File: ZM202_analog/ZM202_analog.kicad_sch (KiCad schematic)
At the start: 2 parts, among them U2 LM324

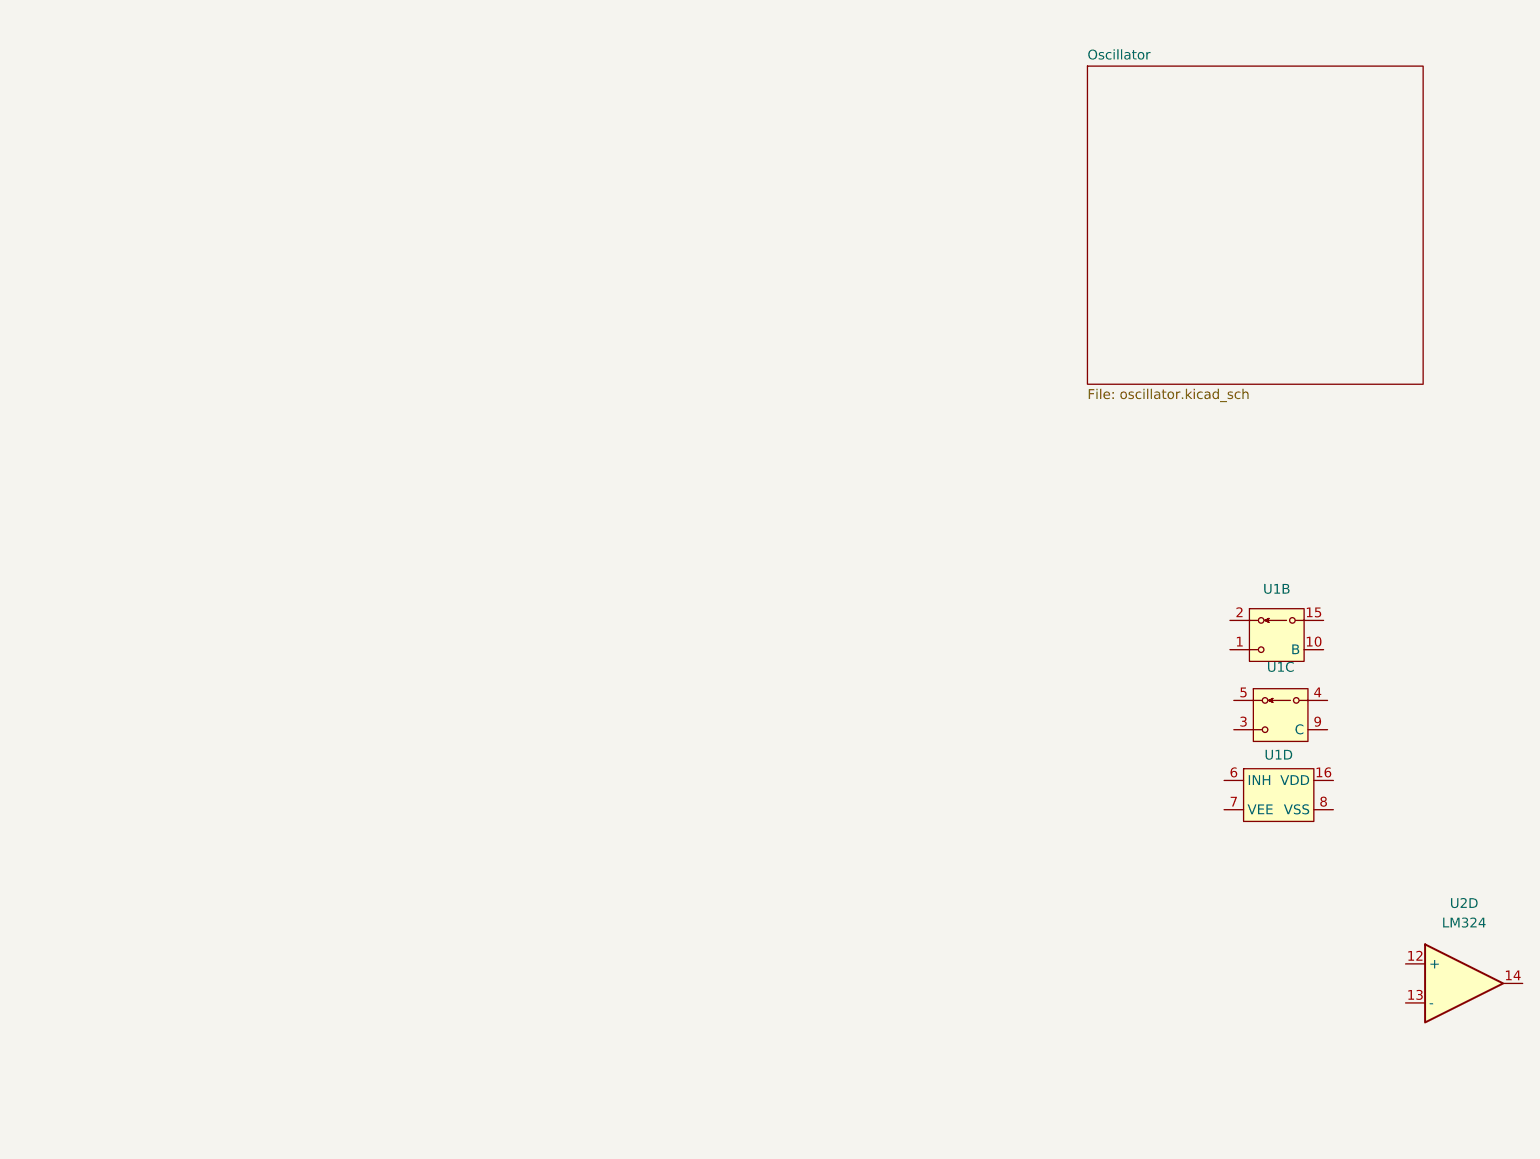
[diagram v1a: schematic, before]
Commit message: Started with the analog part, placing the symbols.
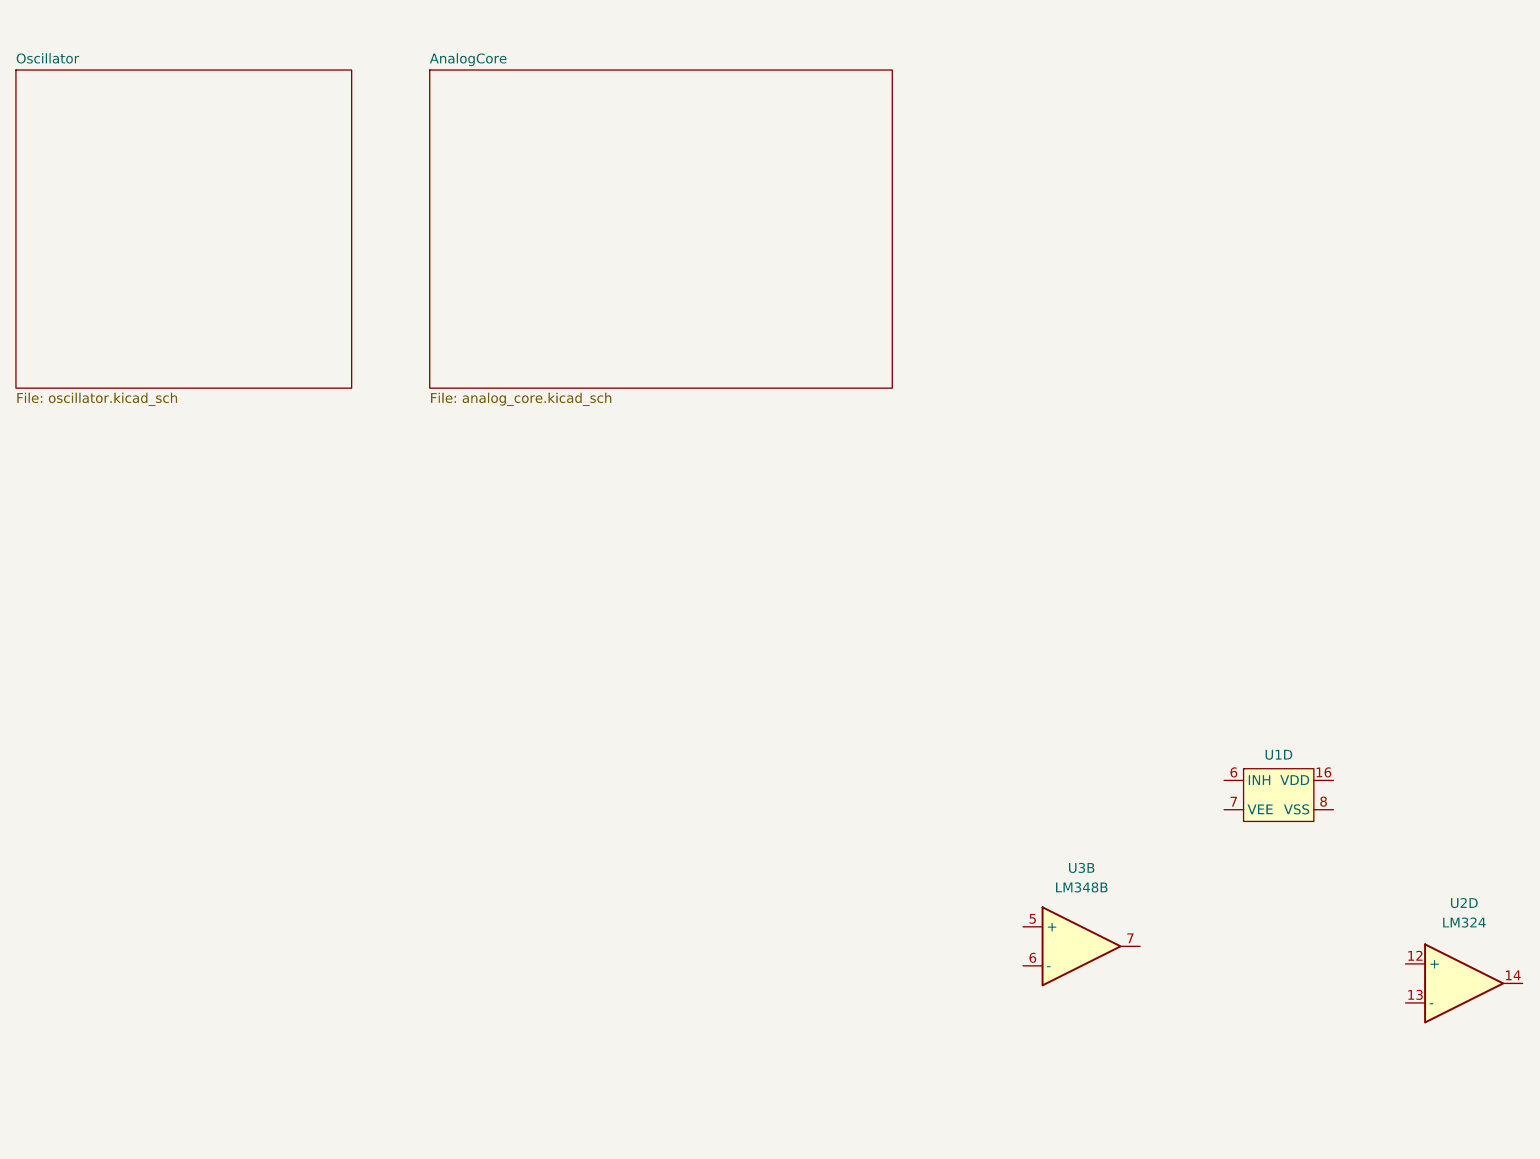
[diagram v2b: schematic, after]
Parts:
- removed unit 3 of U1
- removed unit 2 of U1
- added U3: LM348B, Package_SO:SO-8_3.9x4.9mm_P1.27mm, symbol Jojos_Lib:LM348B
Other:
- added sheet AnalogCore (analog_core.kicad_sch)
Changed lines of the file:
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@@
 (kicad_sch (version 20230121) (generator eeschema)
   (paper "A4")
-  (symbol (lib_id "Jojos_Lib:CD4053") (at 199.898 117.094 0) (unit 3)
+  (symbol (lib_id "Jojos_Lib:LM348B") (at 173.736 147.066 0) (unit 2)
     (in_bom yes) (on_board yes) (dnp no) (fields_autoplaced)
-    (property "Reference" "U1" (at 200.914 110.744 0)
+    (property "Reference" "U3" (at 175.006 136.906 0)
       (effects (font (size 1.27 1.27)))
     )
-    (property "Value" "~" (at 198.374 117.348 0)
+    (property "Value" "LM348B" (at 175.006 139.446 0)
       (effects (font (size 1.27 1.27)))
     )
-    (property "Footprint" "Package_SO:SOIC-16W_5.3x10.2mm_P1.27mm" (at 198.374 117.348 0)
+    (property "Footprint" "Package_SO:SO-8_3.9x4.9mm_P1.27mm" (at 173.736 147.066 0)
       (effects (font (size 1.27 1.27)) hide)
     )
-    (property "Datasheet" "" (at 198.374 117.348 0)
+    (property "Datasheet" "" (at 173.736 147.066 0)
       (effects (font (size 1.27 1.27)) hide)
     )
-    (property "Mouser Part Number" "595-CD4053BM96G3" (at 199.898 117.094 0)
+    (property "Mouser Part Number" "595-LM358BAIDR " (at 173.736 147.066 0)
       (effects (font (size 1.27 1.27)) hide)
     )
-    (pin "11")
-    (pin "12")
-    (pin "13")
-    (pin "14")
     (pin "1")
-    (pin "10")
-    (pin "15")
     (pin "2")
     (pin "3")
     (pin "4")
+    (pin "8")
     (pin "5")
-    (pin "9")
-    (pin "16")
     (pin "6")
     (pin "7")
-    (pin "8")
     (instances
       (project "ZM202_analog"
+        (path "/99a04650-e6a5-4da0-b985-3216476cb3cd/a9b89a8e-6c2e-4f11-9fd4-3a829ee04b26"
+          (reference "U3") (unit 2)
+        )
         (path "/99a04650-e6a5-4da0-b985-3216476cb3cd"
-          (reference "U1") (unit 3)
+          (reference "U3") (unit 2)
         )
       )
@@
     )
   )
-  (symbol (lib_id "Jojos_Lib:CD4053") (at 199.898 106.426 0) (unit 2)
-    (in_bom yes) (on_board yes) (dnp no) (fields_autoplaced)
-    (property "Reference" "U1" (at 200.406 100.584 0)
-      (effects (font (size 1.27 1.27)))
-    )
-    (property "Value" "~" (at 198.374 106.68 0)
-      (effects (font (size 1.27 1.27)))
-    )
-    (property "Footprint" "Package_SO:SOIC-16W_5.3x10.2mm_P1.27mm" (at 198.374 106.68 0)
-      (effects (font (size 1.27 1.27)) hide)
-    )
-    (property "Datasheet" "" (at 198.374 106.68 0)
-      (effects (font (size 1.27 1.27)) hide)
-    )
-    (property "Mouser Part Number" "595-CD4053BM96G3" (at 199.898 106.426 0)
-      (effects (font (size 1.27 1.27)) hide)
-    )
-    (pin "11")
-    (pin "12")
-    (pin "13")
-    (pin "14")
-    (pin "1")
-    (pin "10")
-    (pin "15")
-    (pin "2")
-    (pin "3")
-    (pin "4")
-    (pin "5")
-    (pin "9")
-    (pin "16")
-    (pin "6")
-    (pin "7")
-    (pin "8")
-    (instances
-      (project "ZM202_analog"
-        (path "/99a04650-e6a5-4da0-b985-3216476cb3cd"
-          (reference "U1") (unit 2)
-        )
-      )
-    )
-  )
   (symbol (lib_id "Jojos_Lib:CD4053") (at 200.66 127 0) (unit 4)
     (in_bom yes) (on_board yes) (dnp no) (fields_autoplaced)
@@
     )
   )
-  (sheet (at 175.768 32.512) (size 43.688 41.402) (fields_autoplaced)
+  (sheet (at 36.322 33.02) (size 43.688 41.402) (fields_autoplaced)
     (stroke (width 0.1524) (type solid))
     (fill (color 0 0 0 0.0000))
-    (property "Sheetname" "Oscillator" (at 175.768 31.8004 0)
+    (property "Sheetname" "Oscillator" (at 36.322 32.3084 0)
       (effects (font (size 1.27 1.27)) (justify left bottom))
     )
-    (property "Sheetfile" "oscillator.kicad_sch" (at 175.768 74.4986 0)
+    (property "Sheetfile" "oscillator.kicad_sch" (at 36.322 75.0066 0)
       (effects (font (size 1.27 1.27)) (justify left top))
     )
@@
       )
     )
+  )
+  (sheet (at 90.17 33.02) (size 60.198 41.402) (fields_autoplaced)
+    (stroke (width 0.1524) (type solid))
+    (fill (color 0 0 0 0.0000))
+    (property "Sheetname" "AnalogCore" (at 90.17 32.3084 0)
+      (effects (font (size 1.27 1.27)) (justify left bottom))
+    )
+    (property "Sheetfile" "analog_core.kicad_sch" (at 90.17 75.0066 0)
+      (effects (font (size 1.27 1.27)) (justify left top))
+    )
+    (instances
+      (project "ZM202_analog"
+        (path "/99a04650-e6a5-4da0-b985-3216476cb3cd" (page "3"))
+      )
+    )

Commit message: Wired analog part.
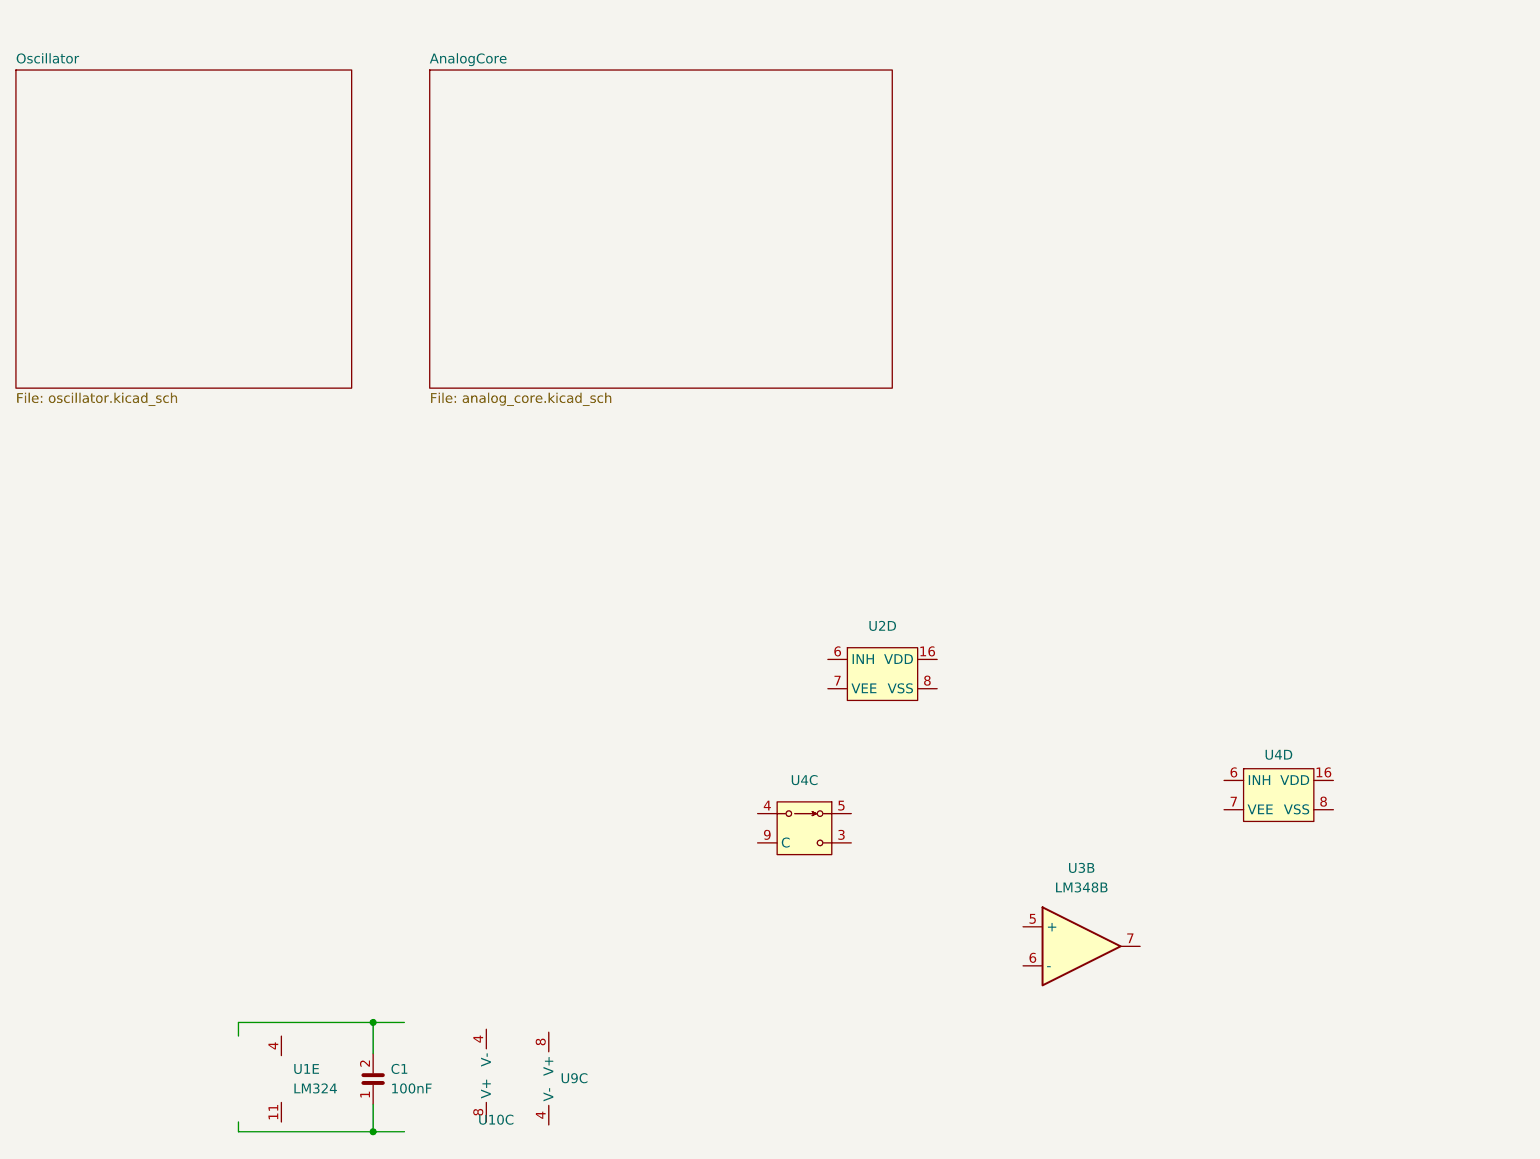
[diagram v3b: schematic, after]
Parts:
- removed U2: LM324, Package_SO:SO-14_3.9x8.65mm_P1.27mm, symbol Jojos_Lib:LM324ADR
- added C1: C0603_100nF_25V, Capacitor_SMD:C_0603_1608Metric, symbol Jojos_Lib:C0603_100nF_25V
- added U1: LM324, Package_SO:SO-14_3.9x8.65mm_P1.27mm, symbol Jojos_Lib:LM324ADR
- added U10, U9: ~, Package_SO:SO-8_3.9x4.9mm_P1.27mm, symbol Jojos_Lib:TLC2272CD
- added U2: ~, Package_SO:SOIC-16W_5.3x10.2mm_P1.27mm, symbol Jojos_Lib:CD4053
- added unit 3 of U4
- renumbered U1 to U4

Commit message: Started placing symbols for the PLL-part.
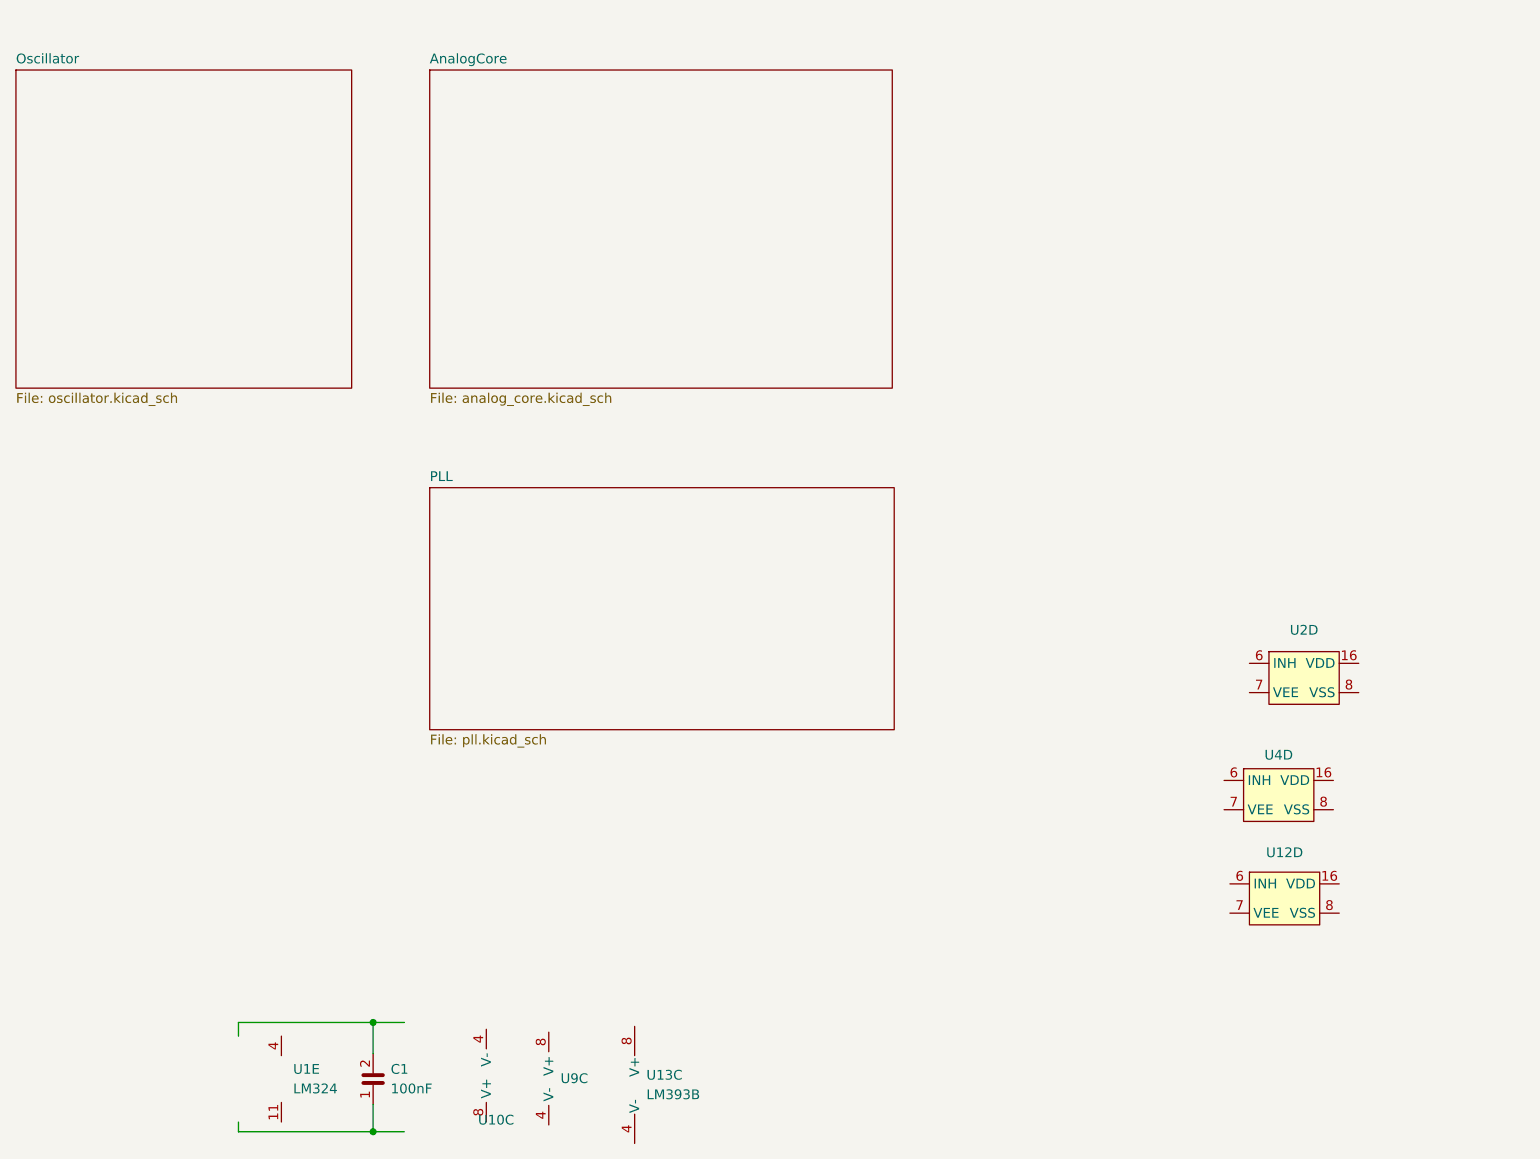
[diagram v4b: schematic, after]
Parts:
- removed U3: LM348B, Package_SO:SO-8_3.9x4.9mm_P1.27mm, symbol Jojos_Lib:LM348B
- removed unit 3 of U4
- added U12: ~, Package_SO:SOIC-16W_5.3x10.2mm_P1.27mm, symbol Jojos_Lib:CD4053
- added U13: LM393B, Package_SO:SO-8_3.9x4.9mm_P1.27mm, symbol Jojos_Lib:LM393B
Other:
- added sheet PLL (pll.kicad_sch)
- moved on the sheet: U2D
